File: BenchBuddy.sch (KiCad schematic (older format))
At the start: 0 parts

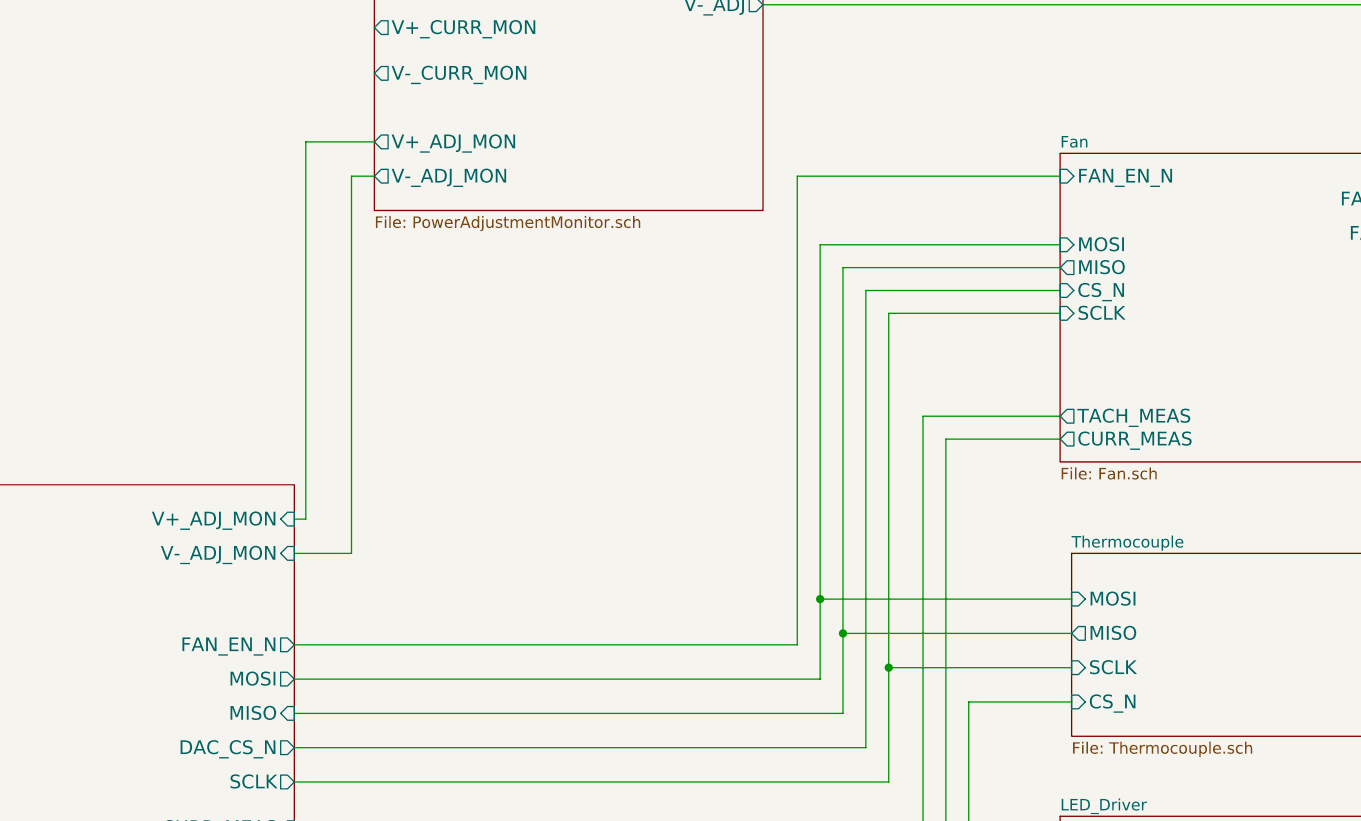
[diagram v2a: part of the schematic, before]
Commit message: Fan/Current Module Refactoring
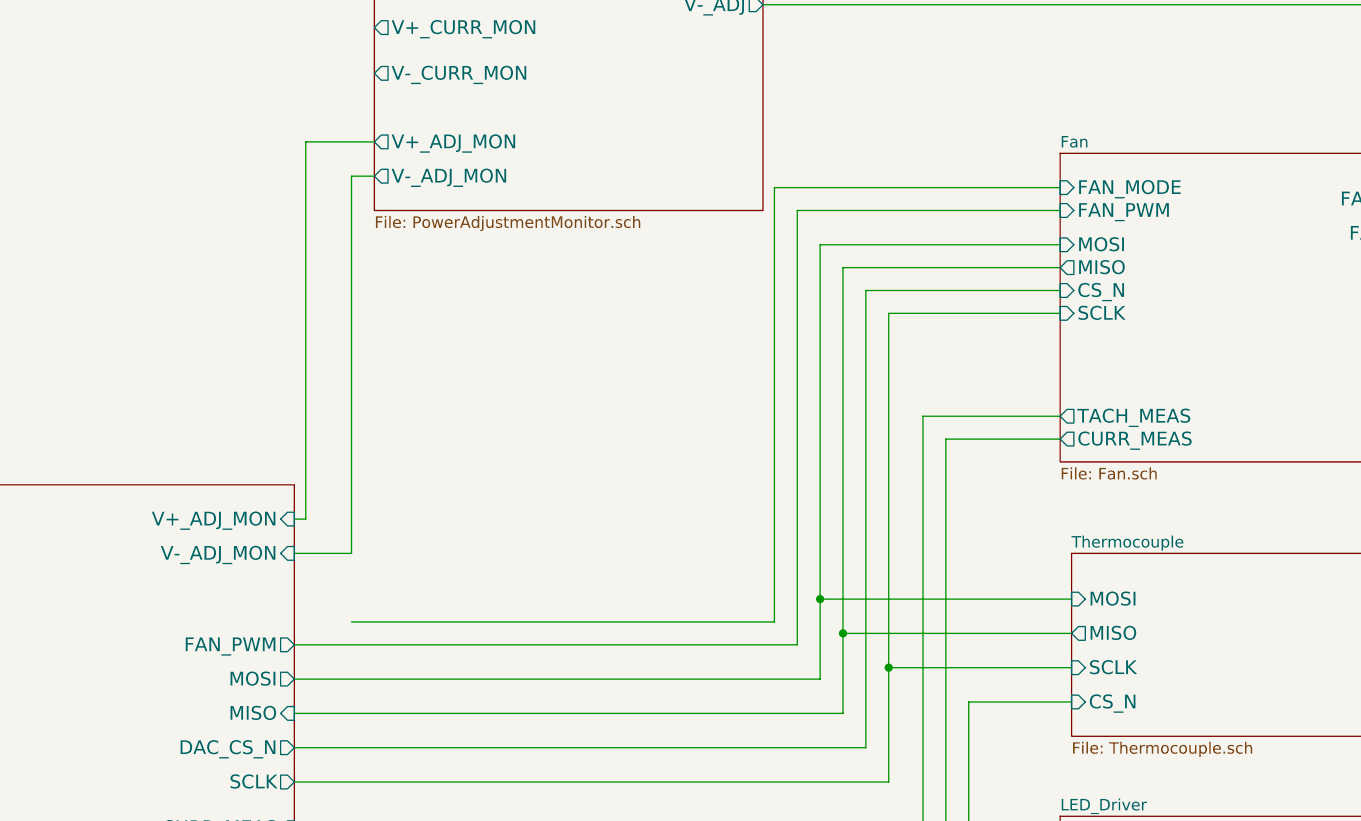
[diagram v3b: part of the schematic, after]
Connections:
- wire segments 50 -> 53
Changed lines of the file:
@@
-EESchema Schematic File Version 2  date 9/22/2013 9:40:39 PM
+EESchema Schematic File Version 2  date 9/25/2013 9:41:10 PM
 LIBS:power
 LIBS:device
@@
 Sheet 1 9
 Title "noname.sch"
-Date "23 sep 2013"
+Date "26 sep 2013"
 Rev ""
 Comp ""
@@
 F7 "TACH_IN" I R 9500 3050 60
 F8 "TACH_MEAS" O L 7750 3100 60
-F9 "FAN_EN_N" I L 7750 2050 60
-F10 "CURR_MEAS" O L 7750 3200 60
-F11 "FAN_OUT-" O R 9500 2300 60
+F9 "CURR_MEAS" O L 7750 3200 60
+F10 "FAN_OUT-" O R 9500 2300 60
+F11 "FAN_PWM" I L 7750 2200 60
+F12 "FAN_MODE" I L 7750 2100 60
 $EndSheet
 $Sheet
@@
 F13 "RELAY_NC" B L 10150 6300 60
 $EndSheet
+Wire Wire Line
+	10150 1100 6450 1100
+Wire Wire Line
+	6450 1300 10150 1300
+Wire Wire Line
+	9500 2150 10150 2150
+Wire Wire Line
+	10150 2300 9500 2300
+Wire Wire Line
+	9500 3050 10150 3050
+Wire Wire Line
+	9500 6000 10150 6000
+Wire Wire Line
+	10150 6150 9500 6150
+Wire Wire Line
+	9500 6300 10150 6300
+Wire Wire Line
+	4400 3550 4450 3550
+Wire Wire Line
+	4450 3550 4450 1900
+Wire Wire Line
+	4450 1900 4750 1900
+Wire Wire Line
+	4400 3700 4650 3700
+Wire Wire Line
+	4650 3700 4650 2050
+Wire Wire Line
+	4650 2050 4750 2050
+Wire Wire Line
+	4400 4100 6600 4100
+Wire Wire Line
+	6600 4100 6600 2200
+Wire Wire Line
+	6600 2200 7750 2200
+Wire Wire Line
+	7750 2350 6700 2350
+Wire Wire Line
+	6700 2350 6700 4250
+Wire Wire Line
+	6700 4250 4400 4250
+Wire Wire Line
+	7750 2450 6800 2450
+Wire Wire Line
+	6800 2450 6800 4400
+Wire Wire Line
+	6800 4400 4400 4400
+Wire Wire Line
+	7750 2550 6900 2550
+Wire Wire Line
+	6900 2550 6900 4550
+Wire Wire Line
+	7000 2650 7000 4700
+Wire Wire Line
+	7000 4700 4400 4700
+Wire Wire Line
+	7750 3100 7150 3100
+Wire Wire Line
+	7150 3100 7150 4900
+Wire Wire Line
+	7150 4900 4400 4900
+Wire Wire Line
+	7750 3200 7250 3200
+Wire Wire Line
+	7250 3200 7250 5050
+Wire Wire Line
+	7250 5050 4400 5050
+Wire Wire Line
+	7800 3900 6700 3900
+Connection ~ 6700 3900
+Wire Wire Line
+	7800 4050 6800 4050
+Connection ~ 6800 4050
+Wire Wire Line
+	6900 4550 4400 4550
+Wire Wire Line
+	7800 4350 7350 4350
+Wire Wire Line
+	7350 4350 7350 5300
+Wire Wire Line
+	7350 5300 4400 5300
+Wire Wire Line
+	4450 5800 7500 5800
+Wire Wire Line
+	7500 5800 7500 5050
+Wire Wire Line
+	7500 5050 7750 5050
+Wire Wire Line
+	7750 6100 4400 6100
+Wire Wire Line
+	4400 6250 7750 6250
+Wire Wire Line
+	10150 3900 9500 3900
+Wire Wire Line
+	10150 4050 9500 4050
+Wire Wire Line
+	10150 5150 9500 5150
+Wire Wire Line
+	9500 5000 10150 5000
+Wire Wire Line
+	7750 2650 7000 2650
+Wire Wire Line
+	7800 4200 7000 4200
+Connection ~ 7000 4200
 $Sheet
 S 2800 3400 1600 3150
@@
 F6 "RELAY+" O R 4400 6100 60
 F7 "RELAY-" O R 4400 6250 60
-F8 "FAN_EN_N" O R 4400 4100 60
-F9 "CURR_MEAS" I R 4400 4900 60
-F10 "V+_ADJ_MON" I R 4400 3550 60
-F11 "V-_ADJ_MON" I R 4400 3700 60
-F12 "LED_EN_PWM" O R 4400 5800 60
-F13 "DAC_CS_N" O R 4400 4550 60
-F14 "ADC_CS_N" O R 4400 5300 60
-$EndSheet
-Wire Wire Line
-	10150 1100 6450 1100
-Wire Wire Line
-	6450 1300 10150 1300
-Wire Wire Line
-	9500 2150 10150 2150
-Wire Wire Line
-	10150 2300 9500 2300
-Wire Wire Line
-	9500 3050 10150 3050
-Wire Wire Line
-	9500 6000 10150 6000
-Wire Wire Line
-	10150 6150 9500 6150
-Wire Wire Line
-	9500 6300 10150 6300
-Wire Wire Line
-	4400 3550 4450 3550
-Wire Wire Line
-	4450 3550 4450 1900
-Wire Wire Line
-	4450 1900 4750 1900
-Wire Wire Line
-	4400 3700 4650 3700
-Wire Wire Line
-	4650 3700 4650 2050
-Wire Wire Line
-	4650 2050 4750 2050
-Wire Wire Line
-	4400 4100 6600 4100
-Wire Wire Line
-	6600 4100 6600 2050
-Wire Wire Line
-	6600 2050 7750 2050
-Wire Wire Line
-	7750 2350 6700 2350
-Wire Wire Line
-	6700 2350 6700 4250
-Wire Wire Line
-	6700 4250 4400 4250
-Wire Wire Line
-	7750 2450 6800 2450
-Wire Wire Line
-	6800 2450 6800 4400
-Wire Wire Line
-	6800 4400 4400 4400
-Wire Wire Line
-	7750 2550 6900 2550
-Wire Wire Line
-	6900 2550 6900 4550
-Wire Wire Line
-	7000 2650 7000 4700
-Wire Wire Line
-	7000 4700 4400 4700
-Wire Wire Line
-	7750 3100 7150 3100
-Wire Wire Line
-	7150 3100 7150 4900
-Wire Wire Line
-	7150 4900 4400 4900
-Wire Wire Line
-	7750 3200 7250 3200
-Wire Wire Line
-	7250 3200 7250 5050
-Wire Wire Line
-	7250 5050 4400 5050
-Wire Wire Line
-	7800 3900 6700 3900
-Connection ~ 6700 3900
-Wire Wire Line
-	7800 4050 6800 4050
-Connection ~ 6800 4050
-Wire Wire Line
-	6900 4550 4400 4550
-Wire Wire Line
-	7800 4350 7350 4350
-Wire Wire Line
-	7350 4350 7350 5300
-Wire Wire Line
-	7350 5300 4400 5300
-Wire Wire Line
-	4450 5800 7500 5800
-Wire Wire Line
-	7500 5800 7500 5050
-Wire Wire Line
-	7500 5050 7750 5050
-Wire Wire Line
-	7750 6100 4400 6100
-Wire Wire Line
-	4400 6250 7750 6250
-Wire Wire Line
-	10150 3900 9500 3900
-Wire Wire Line
-	10150 4050 9500 4050
-Wire Wire Line
-	10150 5150 9500 5150
-Wire Wire Line
-	9500 5000 10150 5000
-Wire Wire Line
-	7750 2650 7000 2650
-Wire Wire Line
-	7800 4200 7000 4200
-Connection ~ 7000 4200
+F8 "CURR_MEAS" I R 4400 4900 60
+F9 "V+_ADJ_MON" I R 4400 3550 60
+F10 "V-_ADJ_MON" I R 4400 3700 60
+F11 "LED_EN_PWM" O R 4400 5800 60
+F12 "DAC_CS_N" O R 4400 4550 60
+F13 "ADC_CS_N" O R 4400 5300 60
+F14 "FAN_PWM" O R 4400 4100 60
+$EndSheet
+Wire Wire Line
+	7750 2100 6500 2100
+Wire Wire Line
+	6500 2100 6500 4000
+Wire Wire Line
+	6500 4000 4650 4000
 $EndSCHEMATC

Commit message: Fan/Current Module 2
Wasn't sure if all of the last changes made it into the commit.
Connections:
- wire segments 53 -> 58
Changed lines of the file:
@@
-EESchema Schematic File Version 2  date 9/25/2013 9:41:10 PM
+EESchema Schematic File Version 2  date 9/25/2013 9:42:53 PM
 LIBS:power
 LIBS:device
@@
 	7750 2350 6700 2350
 Wire Wire Line
-	6700 2350 6700 4250
+	6700 2350 6700 3900
+Wire Wire Line
+	6700 3900 6700 4250
 Wire Wire Line
 	6700 4250 4400 4250
@@
 	7750 2450 6800 2450
 Wire Wire Line
-	6800 2450 6800 4400
+	6800 2450 6800 4050
+Wire Wire Line
+	6800 4050 6800 4400
 Wire Wire Line
 	6800 4400 4400 4400
@@
 	6900 2550 6900 4550
 Wire Wire Line
-	7000 2650 7000 4700
+	7000 2650 7000 4200
+Wire Wire Line
+	7000 4200 7000 4700
 Wire Wire Line
 	7000 4700 4400 4700
@@
 F13 "ADC_CS_N" O R 4400 5300 60
 F14 "FAN_PWM" O R 4400 4100 60
+F15 "FAN_MODE" I R 4400 3950 60
 $EndSheet
 Wire Wire Line
 	7750 2100 6500 2100
 Wire Wire Line
-	6500 2100 6500 4000
-Wire Wire Line
-	6500 4000 4650 4000
+	6500 3950 6500 2100
+Wire Wire Line
+	4550 3950 6500 3950
+Wire Wire Line
+	4550 3950 4550 3950
+Wire Wire Line
+	4550 3950 4400 3950
 $EndSCHEMATC

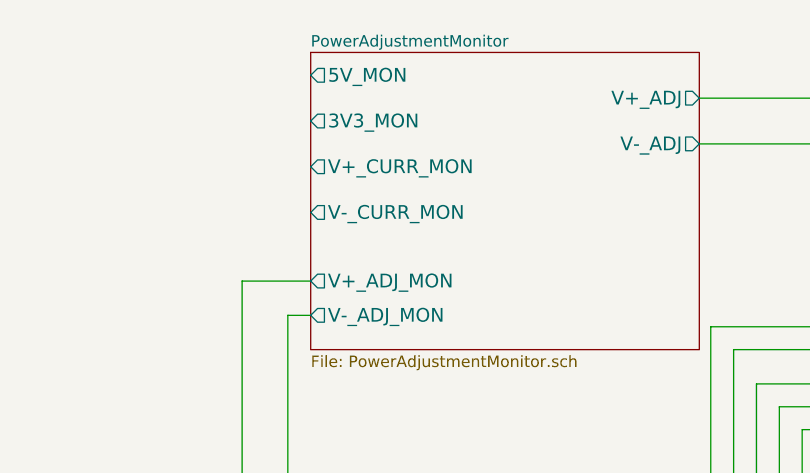
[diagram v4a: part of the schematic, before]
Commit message: Clean Up Arduino Module
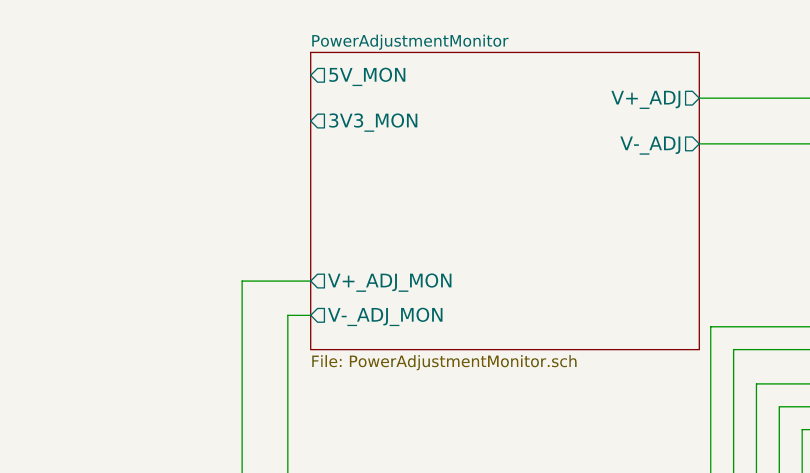
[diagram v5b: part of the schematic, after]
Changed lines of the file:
@@
-EESchema Schematic File Version 2  date 9/25/2013 9:42:53 PM
+EESchema Schematic File Version 2  date 10/6/2013 4:17:57 PM
 LIBS:power
 LIBS:device
@@
 Sheet 1 9
 Title "noname.sch"
-Date "26 sep 2013"
+Date "6 oct 2013"
 Rev ""
 Comp ""
@@
 F6 "V+_ADJ_MON" O L 4750 1900 60
 F7 "V-_ADJ_MON" O L 4750 2050 60
-F8 "V-_CURR_MON" O L 4750 1600 60
-F9 "V+_CURR_MON" O L 4750 1400 60
 $EndSheet
 $Sheet
